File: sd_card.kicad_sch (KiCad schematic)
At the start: 19 parts, among them J1101 DM3AT-SF-PEJM5

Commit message: Update R & L BOM
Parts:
- R1101, R1102, R1103, R1104, R1105, R1106, R1107: footprint (none) -> perfect_footprints:R_0402_1005Metric; Digi-Key Part Number (none) -> P0.0JCT-ND; MPN (none) -> ERJ-2GE0R00X; Manufacturer (none) -> Panasonic Electronic Components
- R1108: Digi-Key Part Number (none) -> P100KLCT-ND; MPN (none) -> ERJ-2RKF1003X; Manufacturer (none) -> Panasonic Electronic Components
- R1109: Digi-Key Part Number (none) -> P10.0KLCT-ND; MPN (none) -> ERJ-2RKF1002X; Manufacturer (none) -> Panasonic Electronic Components
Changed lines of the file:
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@@
 			)
 		)
-		(property "Footprint" ""
+		(property "Footprint" "perfect_footprints:R_0402_1005Metric"
 			(at 114.3 143.002 90)
 			(effects
@@
 			)
 		)
-		(property "Datasheet" ""
+		(property "Datasheet" "https://industrial.panasonic.com/ww/products/pt/general-purpose-chip-resistors/models/ERJ2GE0R00X"
 			(at 114.3 144.78 0)
 			(effects
@@
 			)
 		)
-		(property "Description" ""
+		(property "Description" "0 Ohms Jumper Chip Resistor 0402 (1005 Metric) Automotive AEC-Q200 Thick Film"
 			(at 114.3 144.78 0)
 			(effects
@@
 			)
 		)
-		(property "MPN" ""
+		(property "MPN" "ERJ-2GE0R00X"
 			(at 114.3 144.78 0)
 			(effects
@@
 			)
 		)
-		(property "Manufacturer" ""
+		(property "Manufacturer" "Panasonic Electronic Components"
 			(at 114.3 144.78 0)
 			(effects
@@
 				)
 				(justify right bottom)
+			)
+		)
+		(property "Digi-Key Part Number" "P0.0JCT-ND"
+			(at 114.3 144.78 90)
+			(effects
+				(font
+					(size 1.27 1.27)
+				)
+				(hide yes)
 			)
 		)
@@
 			)
 		)
-		(property "Datasheet" "https://www.we-online.com/components/products/datasheet/560112116014.pdf"
+		(property "Datasheet" "https://industrial.panasonic.com/cdbs/www-data/pdf/RDA0000/AOA0000C304.pdf"
 			(at 133.35 154.94 0)
 			(effects
@@
 			)
 		)
-		(property "Description" "Resistor"
+		(property "Description" "10 kOhms ±1% 0.1W, 1/10W Chip Resistor 0402 (1005 Metric) Automotive AEC-Q200 Thick Film"
 			(at 133.35 154.94 0)
 			(effects
@@
 			)
 		)
-		(property "MPN" ""
+		(property "MPN" "ERJ-2RKF1002X"
 			(at 133.35 154.94 0)
 			(effects
@@
 			)
 		)
-		(property "Manufacturer" ""
+		(property "Manufacturer" "Panasonic Electronic Components"
 			(at 133.35 154.94 0)
 			(effects
@@
 				)
 				(justify left)
+			)
+		)
+		(property "Digi-Key Part Number" "P10.0KLCT-ND"
+			(at 133.35 154.94 0)
+			(effects
+				(font
+					(size 1.27 1.27)
+				)
+				(hide yes)
 			)
 		)
@@
 			)
 		)
-		(property "Footprint" ""
+		(property "Footprint" "perfect_footprints:R_0402_1005Metric"
 			(at 114.3 140.462 90)
 			(effects
@@
 			)
 		)
-		(property "Datasheet" ""
+		(property "Datasheet" "https://industrial.panasonic.com/ww/products/pt/general-purpose-chip-resistors/models/ERJ2GE0R00X"
 			(at 114.3 142.24 0)
 			(effects
@@
 			)
 		)
-		(property "Description" ""
+		(property "Description" "0 Ohms Jumper Chip Resistor 0402 (1005 Metric) Automotive AEC-Q200 Thick Film"
 			(at 114.3 142.24 0)
 			(effects
@@
 			)
 		)
-		(property "MPN" ""
+		(property "MPN" "ERJ-2GE0R00X"
 			(at 114.3 142.24 0)
 			(effects
@@
 			)
 		)
-		(property "Manufacturer" ""
+		(property "Manufacturer" "Panasonic Electronic Components"
 			(at 114.3 142.24 0)
 			(effects
@@
 				)
 				(justify right bottom)
+			)
+		)
+		(property "Digi-Key Part Number" "P0.0JCT-ND"
+			(at 114.3 142.24 90)
+			(effects
+				(font
+					(size 1.27 1.27)
+				)
+				(hide yes)
 			)
 		)
@@
 			)
 		)
-		(property "Footprint" ""
+		(property "Footprint" "perfect_footprints:R_0402_1005Metric"
 			(at 114.3 130.302 90)
 			(effects
@@
 			)
 		)
-		(property "Datasheet" ""
+		(property "Datasheet" "https://industrial.panasonic.com/ww/products/pt/general-purpose-chip-resistors/models/ERJ2GE0R00X"
 			(at 114.3 132.08 0)
 			(effects
@@
 			)
 		)
-		(property "Description" ""
+		(property "Description" "0 Ohms Jumper Chip Resistor 0402 (1005 Metric) Automotive AEC-Q200 Thick Film"
 			(at 114.3 132.08 0)
 			(effects
@@
 			)
 		)
-		(property "MPN" ""
+		(property "MPN" "ERJ-2GE0R00X"
 			(at 114.3 132.08 0)
 			(effects
@@
 			)
 		)
-		(property "Manufacturer" ""
+		(property "Manufacturer" "Panasonic Electronic Components"
 			(at 114.3 132.08 0)
 			(effects
@@
 				)
 				(justify right bottom)
+			)
+		)
+		(property "Digi-Key Part Number" "P0.0JCT-ND"
+			(at 114.3 132.08 90)
+			(effects
+				(font
+					(size 1.27 1.27)
+				)
+				(hide yes)
 			)
 		)
@@
 			)
 		)
-		(property "Footprint" ""
+		(property "Footprint" "perfect_footprints:R_0402_1005Metric"
 			(at 114.3 125.222 90)
 			(effects
@@
 			)
 		)
-		(property "Datasheet" ""
+		(property "Datasheet" "https://industrial.panasonic.com/ww/products/pt/general-purpose-chip-resistors/models/ERJ2GE0R00X"
 			(at 114.3 127 0)
 			(effects
@@
 			)
 		)
-		(property "Description" ""
+		(property "Description" "0 Ohms Jumper Chip Resistor 0402 (1005 Metric) Automotive AEC-Q200 Thick Film"
 			(at 114.3 127 0)
 			(effects
@@
 			)
 		)
-		(property "MPN" ""
+		(property "MPN" "ERJ-2GE0R00X"
 			(at 114.3 127 0)
 			(effects
@@
 			)
 		)
-		(property "Manufacturer" ""
+		(property "Manufacturer" "Panasonic Electronic Components"
 			(at 114.3 127 0)
 			(effects
@@
 				)
 				(justify right bottom)
+			)
+		)
+		(property "Digi-Key Part Number" "P0.0JCT-ND"
+			(at 114.3 127 90)
+			(effects
+				(font
+					(size 1.27 1.27)
+				)
+				(hide yes)
 			)
 		)
@@
 			)
 		)
-		(property "Footprint" ""
+		(property "Footprint" "perfect_footprints:R_0402_1005Metric"
 			(at 114.3 145.542 90)
 			(effects
@@
 			)
 		)
-		(property "Datasheet" ""
+		(property "Datasheet" "https://industrial.panasonic.com/ww/products/pt/general-purpose-chip-resistors/models/ERJ2GE0R00X"
 			(at 114.3 147.32 0)
 			(effects
@@
 			)
 		)
-		(property "Description" ""
+		(property "Description" "0 Ohms Jumper Chip Resistor 0402 (1005 Metric) Automotive AEC-Q200 Thick Film"
 			(at 114.3 147.32 0)
 			(effects
@@
 			)
 		)
-		(property "MPN" ""
+		(property "MPN" "ERJ-2GE0R00X"
 			(at 114.3 147.32 0)
 			(effects
@@
 			)
 		)
-		(property "Manufacturer" ""
+		(property "Manufacturer" "Panasonic Electronic Components"
 			(at 114.3 147.32 0)
 			(effects
@@
 				)
 				(justify right bottom)
+			)
+		)
+		(property "Digi-Key Part Number" "P0.0JCT-ND"
+			(at 114.3 147.32 90)
+			(effects
+				(font
+					(size 1.27 1.27)
+				)
+				(hide yes)
 			)
 		)
@@
 			)
 		)
-		(property "Footprint" ""
+		(property "Footprint" "perfect_footprints:R_0402_1005Metric"
 			(at 114.3 135.382 90)
 			(effects
@@
 			)
 		)
-		(property "Datasheet" ""
+		(property "Datasheet" "https://industrial.panasonic.com/ww/products/pt/general-purpose-chip-resistors/models/ERJ2GE0R00X"
 			(at 114.3 137.16 0)
 			(effects
@@
 			)
 		)
-		(property "Description" ""
+		(property "Description" "0 Ohms Jumper Chip Resistor 0402 (1005 Metric) Automotive AEC-Q200 Thick Film"
 			(at 114.3 137.16 0)
 			(effects
@@
 			)
 		)
-		(property "MPN" ""
+		(property "MPN" "ERJ-2GE0R00X"
 			(at 114.3 137.16 0)
 			(effects
@@
 			)
 		)
-		(property "Manufacturer" ""
+		(property "Manufacturer" "Panasonic Electronic Components"
 			(at 114.3 137.16 0)
 			(effects
@@
 				)
 				(justify right bottom)
+			)
+		)
+		(property "Digi-Key Part Number" "P0.0JCT-ND"
+			(at 114.3 137.16 90)
+			(effects
+				(font
+					(size 1.27 1.27)
+				)
+				(hide yes)
 			)
 		)
@@
 			)
 		)
-		(property "Footprint" ""
+		(property "Footprint" "perfect_footprints:R_0402_1005Metric"
 			(at 114.3 127.762 90)
 			(effects
@@
 			)
 		)
-		(property "Datasheet" ""
+		(property "Datasheet" "https://industrial.panasonic.com/ww/products/pt/general-purpose-chip-resistors/models/ERJ2GE0R00X"
 			(at 114.3 129.54 0)
 			(effects
@@
 			)
 		)
-		(property "Description" ""
+		(property "Description" "0 Ohms Jumper Chip Resistor 0402 (1005 Metric) Automotive AEC-Q200 Thick Film"
 			(at 114.3 129.54 0)
 			(effects
@@
 			)
 		)
-		(property "MPN" ""
+		(property "MPN" "ERJ-2GE0R00X"
 			(at 114.3 129.54 0)
 			(effects
@@
 			)
 		)
-		(property "Manufacturer" ""
+		(property "Manufacturer" "Panasonic Electronic Components"
 			(at 114.3 129.54 0)
 			(effects
@@
 				)
 				(justify right bottom)
+			)
+		)
+		(property "Digi-Key Part Number" "P0.0JCT-ND"
+			(at 114.3 129.54 90)
+			(effects
+				(font
+					(size 1.27 1.27)
+				)
+				(hide yes)
 			)
 		)
@@
 			)
 		)
-		(property "Datasheet" "https://www.we-online.com/components/products/datasheet/560112116014.pdf"
+		(property "Datasheet" "https://industrial.panasonic.com/cdbs/www-data/pdf/RDA0000/AOA0000C304.pdf"
 			(at 127 120.65 0)
 			(effects
@@
 			)
 		)
-		(property "Description" "Resistor"
+		(property "Description" "100 kOhms ±1% 0.1W, 1/10W Chip Resistor 0402 (1005 Metric) Automotive AEC-Q200 Thick Film"
 			(at 127 120.65 0)
 			(effects
@@
 			)
 		)
-		(property "MPN" ""
+		(property "MPN" "ERJ-2RKF1003X"
 			(at 127 120.65 0)
 			(effects
@@
 			)
 		)
-		(property "Manufacturer" ""
+		(property "Manufacturer" "Panasonic Electronic Components"
 			(at 127 120.65 0)
 			(effects
@@
 			)
 		)
+		(property "Digi-Key Part Number" "P100KLCT-ND"
+			(at 127 120.65 0)
+			(effects
+				(font
+					(size 1.27 1.27)
+				)
+				(hide yes)
+			)
+		)

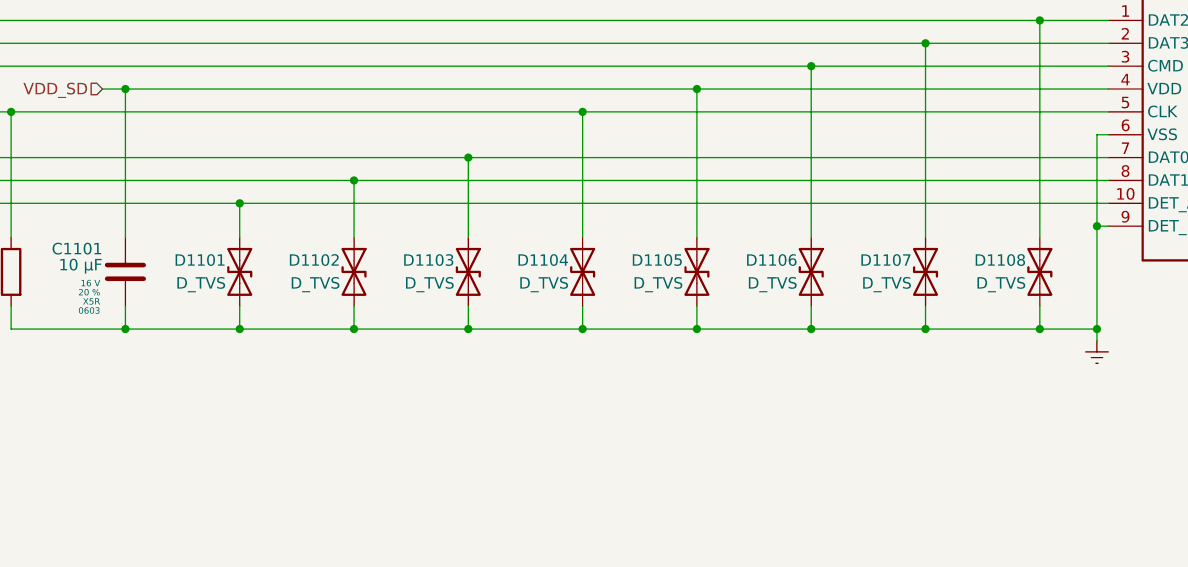
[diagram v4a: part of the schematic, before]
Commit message: Fill BOM info
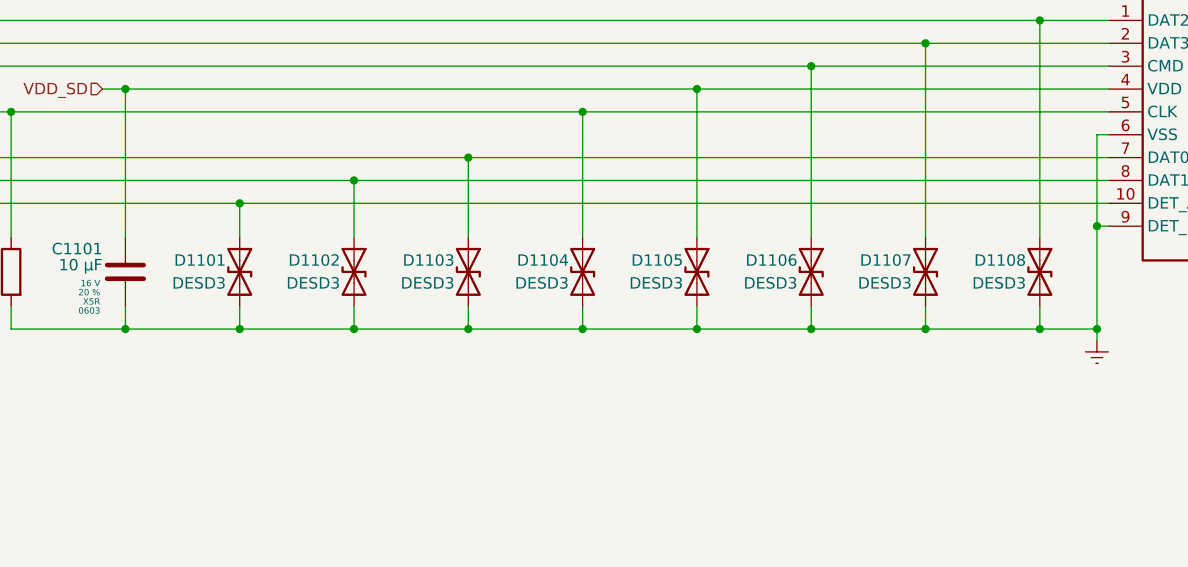
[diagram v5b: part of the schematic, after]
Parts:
- D1101, D1102, D1103, D1104, D1105, D1106, D1107, D1108: value D_TVS -> DESD3; footprint (none) -> Diode_SMD:D_SOD-323; Digi-Key Part Number (none) -> 31-DESD3V3L1BAQ-7CT-ND; MPN (none) -> DESD3V3L1BAQ-7; Manufacturer (none) -> Diodes Incorporated

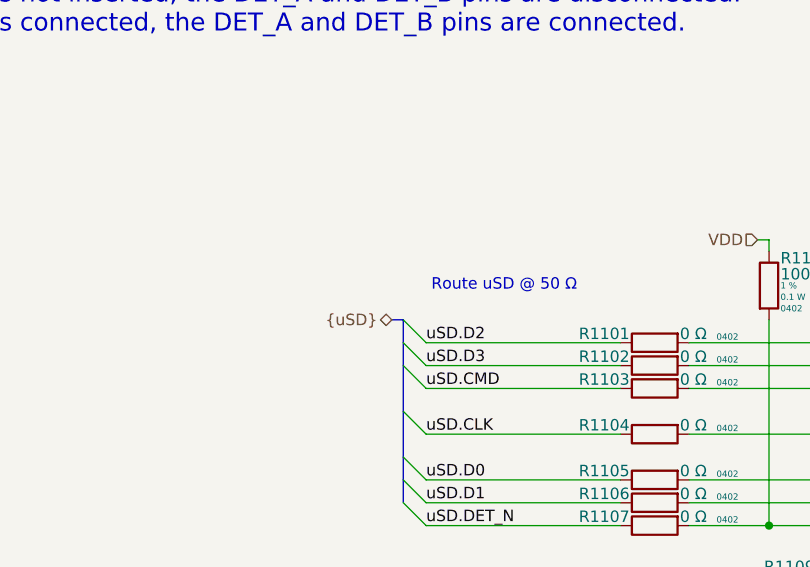
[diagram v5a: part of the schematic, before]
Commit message: Fill BOM information for the rest
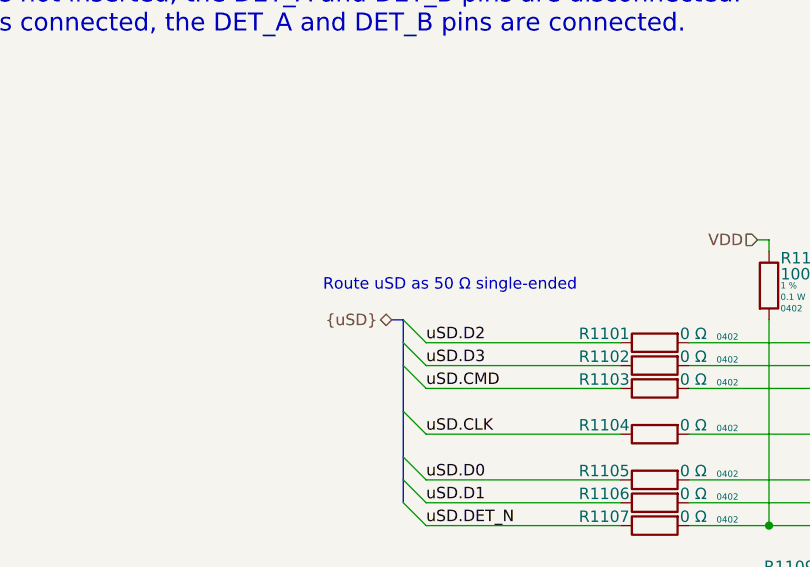
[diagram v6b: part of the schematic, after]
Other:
- note added: "Route uSD as 50 Ω single-ended"
- note removed: "Route uSD @ 50 Ω"
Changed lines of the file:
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@@
 		(rev "v0.0.1")
 	)
-	(text "Route uSD @ 50 Ω"
+	(text "Route uSD as 50 Ω single-ended"
 		(exclude_from_sim no)
 		(at 105.664 120.65 0)

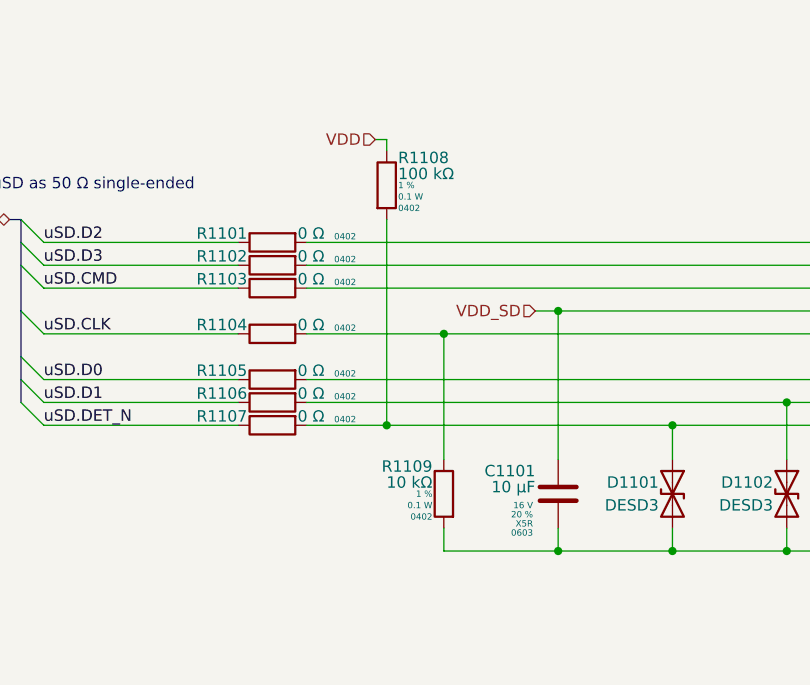
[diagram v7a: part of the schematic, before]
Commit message: 0402 -> 0201 where possible
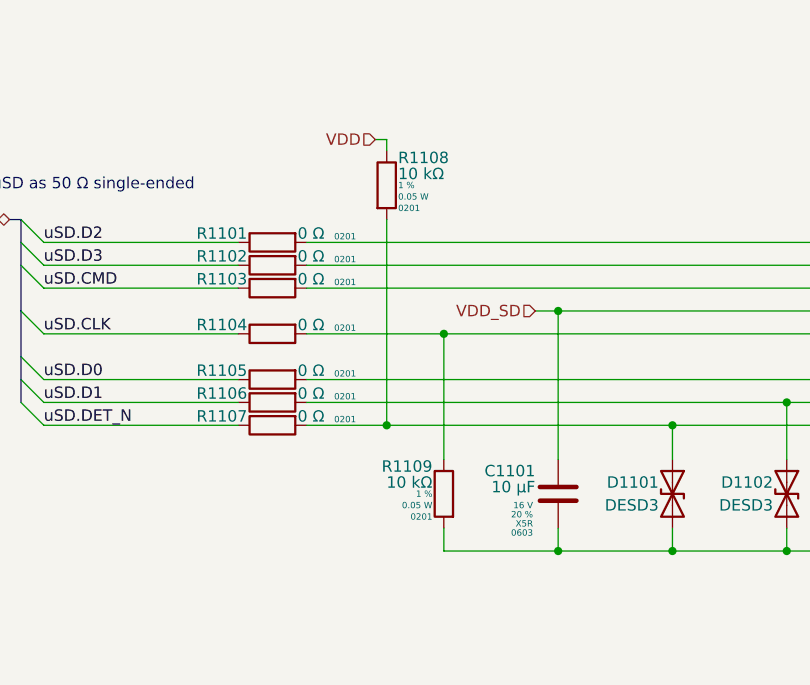
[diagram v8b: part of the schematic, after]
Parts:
- R1101, R1102, R1103, R1104, R1105, R1106, R1107: footprint perfect_footprints:R_0402_1005Metric -> Resistor_SMD:R_0201_0603Metric; Digi-Key Part Number P0.0JCT-ND -> P15979CT-ND; MPN ERJ-2GE0R00X -> ERJ-1GN0R00C; Size 0402 -> 0201
- R1108: value 100 kΩ -> 10 kΩ; footprint perfect_footprints:R_0402_1005Metric -> Resistor_SMD:R_0201_0603Metric; Digi-Key Part Number P100KLCT-ND -> P122414CT-ND; MPN ERJ-2RKF1003X -> ERJ-1GNF1002C; Power rating 0.1 W -> 0.05 W; Size 0402 -> 0201
- R1109: footprint perfect_footprints:R_0402_1005Metric -> Resistor_SMD:R_0201_0603Metric; Digi-Key Part Number P10.0KLCT-ND -> P122414CT-ND; MPN ERJ-2RKF1002X -> ERJ-1GNF1002C; Power rating 0.1 W -> 0.05 W; Size 0402 -> 0201
